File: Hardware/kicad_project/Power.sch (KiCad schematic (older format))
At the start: 11 parts

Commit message: update project with corrected schematic / pcb
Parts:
- removed U?: NCP1117-3.3_SOT223, Package_TO_SOT_SMD:SOT-223-3_TabPin2, symbol Regulator_Linear:NCP1117-3.3_SOT223
- added U7: AMS1117-3.3, TO_SOT_Packages_SMD:SOT-223, symbol Regulator_Linear:AMS1117-3.3
- C57: renamed from C?; footprint RandomJunk:C_0603_nosilk -> Capacitors_SMD:C_0402_NoSilk; LCSC c19702 -> C15525
- C58: renamed from C?; footprint (none) -> Capacitors_SMD:C_0402_NoSilk; LCSC (none) -> C15525
- Q1: renamed from Q?; LCSC c144153 -> C144153
- R16: renamed from R?; footprint Resistors_SMD:R_0603 -> Resistors_SMD:R_0402_NoSilk; LCSC c23162 -> C23162
- R17: renamed from R?; footprint Resistors_SMD:R_0603 -> Resistors_SMD:R_0402_NoSilk; LCSC c21190 -> C11702
- R18: renamed from R?; footprint Resistors_SMD:R_0603 -> Resistors_SMD:R_0402_NoSilk; LCSC c25803 -> C25803
- gave numbers to parts that had none: 4
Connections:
- net +3V3: now also U7.2 (VO)
- net +BATT: now also J7.2 (Pin_2); no longer J7.1 (Pin_1)
- net GND: now also J7.1 (Pin_1), U7.1 (GND); no longer J7.2 (Pin_2)
- net at D53.1 (K), Q1.2 (S): now also U7.3 (VI)
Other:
- moved on the sheet: J7
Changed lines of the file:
@@
 $EndDescr
 $Comp
-L power:+BATT #PWR?
+L power:+BATT #PWR041
 U 1 1 63689321
 P 7300 2550
-F 0 "#PWR?" H 7300 2400 50  0001 C CNN
+F 0 "#PWR041" H 7300 2400 50  0001 C CNN
 F 1 "+BATT" H 7315 2723 50  0000 C CNN
 F 2 "" H 7300 2550 50  0001 C CNN
@@
 	7700 3250 8050 3250
 $Comp
-L power:GND #PWR?
-U 1 1 6368932B
-P 8050 3800
-F 0 "#PWR?" H 8050 3550 50  0001 C CNN
-F 1 "GND" H 8055 3627 50  0000 C CNN
-F 2 "" H 8050 3800 50  0001 C CNN
-F 3 "" H 8050 3800 50  0001 C CNN
-	1    8050 3800
-	1    0    0    -1
-$EndComp
-$Comp
-L Device:C C?
+L Device:C C58
 U 1 1 63689331
 P 8050 3550
-F 0 "C?" H 8165 3596 50  0000 L CNN
+F 0 "C58" H 8165 3596 50  0000 L CNN
 F 1 "10u" H 8165 3505 50  0000 L CNN
-F 2 "" H 8088 3400 50  0001 C CNN
+F 2 "Capacitors_SMD:C_0402_NoSilk" H 8088 3400 50  0001 C CNN
 F 3 "~" H 8050 3550 50  0001 C CNN
+F 4 "C15525" H 8050 3550 50  0001 C CNN "LCSC"
 	1    8050 3550
 	1    0    0    -1
 $EndComp
 $Comp
-L power:+3.3V #PWR?
+L power:+3.3V #PWR045
 U 1 1 63689337
 P 8050 3250
-F 0 "#PWR?" H 8050 3100 50  0001 C CNN
+F 0 "#PWR045" H 8050 3100 50  0001 C CNN
 F 1 "+3.3V" H 8065 3423 50  0000 C CNN
 F 2 "" H 8050 3250 50  0001 C CNN
@@
 $EndComp
 $Comp
-L power:GND #PWR?
+L power:GND #PWR049
 U 1 1 6368933D
 P 7400 3550
-F 0 "#PWR?" H 7400 3300 50  0001 C CNN
+F 0 "#PWR049" H 7400 3300 50  0001 C CNN
 F 1 "GND" H 7405 3377 50  0000 C CNN
 F 2 "" H 7400 3550 50  0001 C CNN
@@
 	6900 3250 7100 3250
 $Comp
-L Regulator_Linear:NCP1117-3.3_SOT223 U?
-U 1 1 63689345
-P 7400 3250
-F 0 "U?" H 7400 3492 50  0000 C CNN
-F 1 "NCP1117-3.3_SOT223" H 7400 3401 50  0000 C CNN
-F 2 "Package_TO_SOT_SMD:SOT-223-3_TabPin2" H 7400 3450 50  0001 C CNN
-F 3 "http://www.onsemi.com/pub_link/Collateral/NCP1117-D.PDF" H 7500 3000 50  0001 C CNN
-	1    7400 3250
-	1    0    0    -1
-$EndComp
-$Comp
-L power:+BATT #PWR?
+L power:+BATT #PWR046
 U 1 1 6368934B
-P 3150 3550
-F 0 "#PWR?" H 3150 3400 50  0001 C CNN
-F 1 "+BATT" H 3165 3723 50  0000 C CNN
-F 2 "" H 3150 3550 50  0001 C CNN
-F 3 "" H 3150 3550 50  0001 C CNN
-	1    3150 3550
-	1    0    0    -1
-$EndComp
-$Comp
-L power:GND #PWR?
+P 3150 3700
+F 0 "#PWR046" H 3150 3550 50  0001 C CNN
+F 1 "+BATT" H 3165 3873 50  0000 C CNN
+F 2 "" H 3150 3700 50  0001 C CNN
+F 3 "" H 3150 3700 50  0001 C CNN
+	1    3150 3700
+	-1   0    0    1
+$EndComp
+$Comp
+L power:GND #PWR050
 U 1 1 63689351
-P 3150 3650
-F 0 "#PWR?" H 3150 3400 50  0001 C CNN
-F 1 "GND" H 3155 3477 50  0000 C CNN
-F 2 "" H 3150 3650 50  0001 C CNN
-F 3 "" H 3150 3650 50  0001 C CNN
-	1    3150 3650
-	1    0    0    -1
-$EndComp
-$Comp
-L Connector_Generic:Conn_01x02 J?
+P 3150 3600
+F 0 "#PWR050" H 3150 3350 50  0001 C CNN
+F 1 "GND" H 3155 3427 50  0000 C CNN
+F 2 "" H 3150 3600 50  0001 C CNN
+F 3 "" H 3150 3600 50  0001 C CNN
+	1    3150 3600
+	-1   0    0    1
+$EndComp
+$Comp
+L Connector_Generic:Conn_01x02 J7
 U 1 1 63689357
-P 3350 3550
-F 0 "J?" H 3430 3542 50  0000 L CNN
-F 1 "battery" H 3430 3451 50  0000 L CNN
-F 2 "Connectors_JST:JST_PH_B2B-PH-SM4-TB_02x2.00mm_Straight" H 3350 3550 50  0001 C CNN
-F 3 "~" H 3350 3550 50  0001 C CNN
-	1    3350 3550
-	1    0    0    -1
-$EndComp
-$Comp
-L Device:R_US R?
+P 3350 3600
+F 0 "J7" H 3430 3592 50  0000 L CNN
+F 1 "battery" H 3430 3501 50  0000 L CNN
+F 2 "Connectors_JST:JST_PH_B2B-PH-SM4-TB_02x2.00mm_Straight" H 3350 3600 50  0001 C CNN
+F 3 "~" H 3350 3600 50  0001 C CNN
+	1    3350 3600
+	1    0    0    -1
+$EndComp
+$Comp
+L Device:R_US R18
 U 1 1 6368935E
 P 6550 3400
-F 0 "R?" V 6345 3400 50  0000 C CNN
+F 0 "R18" V 6345 3400 50  0000 C CNN
 F 1 "100k" V 6436 3400 50  0000 C CNN
-F 2 "Resistors_SMD:R_0603" V 6590 3390 50  0001 C CNN
+F 2 "Resistors_SMD:R_0402_NoSilk" V 6590 3390 50  0001 C CNN
 F 3 "~" H 6550 3400 50  0001 C CNN
-F 4 "c25803" H 6550 3400 50  0001 C CNN "LCSC"
+F 4 "C25803" H 6550 3400 50  0001 C CNN "LCSC"
 	1    6550 3400
 	-1   0    0    1
@@
 Connection ~ 6550 3250
 $Comp
-L power:GND #PWR?
+L power:GND #PWR048
 U 1 1 63689365
 P 6550 3550
-F 0 "#PWR?" H 6550 3300 50  0001 C CNN
+F 0 "#PWR048" H 6550 3300 50  0001 C CNN
 F 1 "GND" H 6555 3377 50  0000 C CNN
 F 2 "" H 6550 3550 50  0001 C CNN
@@
 $EndComp
 $Comp
-L Device:R_US R?
+L Device:R_US R16
 U 1 1 6368936C
 P 4250 3350
-F 0 "R?" V 4045 3350 50  0000 C CNN
+F 0 "R16" V 4045 3350 50  0000 C CNN
 F 1 "4.7k" V 4136 3350 50  0000 C CNN
-F 2 "Resistors_SMD:R_0603" V 4290 3340 50  0001 C CNN
+F 2 "Resistors_SMD:R_0402_NoSilk" V 4290 3340 50  0001 C CNN
 F 3 "~" H 4250 3350 50  0001 C CNN
-F 4 "c23162" H 4250 3350 50  0001 C CNN "LCSC"
+F 4 "C23162" H 4250 3350 50  0001 C CNN "LCSC"
 	1    4250 3350
 	0    1    1    0
@@
 	4100 3350 4100 3650
 $Comp
-L dk_PMIC-Battery-Chargers:MCP73831T-2ATI_OT U?
+L dk_PMIC-Battery-Chargers:MCP73831T-2ATI_OT U6
 U 1 1 6368937D
 P 4800 3250
-F 0 "U?" H 4800 3653 60  0000 C CNN
+F 0 "U6" H 4800 3653 60  0000 C CNN
 F 1 "MCP73831T-2ATI_OT" H 4800 3547 60  0000 C CNN
 F 2 "TO_SOT_Packages_SMD:SOT-23-5" H 5000 3450 60  0001 L CNN
@@
 	6550 2850 6550 3250
 $Comp
-L Device:D_Schottky D?
+L Device:D_Schottky D53
 U 1 1 6368938B
 P 6700 3250
-F 0 "D?" H 6700 3034 50  0000 C CNN
+F 0 "D53" H 6700 3034 50  0000 C CNN
 F 1 "D_Schottky" H 6700 3125 50  0000 C CNN
 F 2 "Diodes_SMD:D_SMA" H 6700 3250 50  0001 C CNN
@@
 $EndComp
 $Comp
-L dk_Transistors-FETs-MOSFETs-Single:DMG2305UX-13 Q?
+L dk_Transistors-FETs-MOSFETs-Single:DMG2305UX-13 Q1
 U 1 1 6368939B
 P 7300 2750
-F 0 "Q?" H 7408 2803 60  0000 L CNN
+F 0 "Q1" H 7408 2803 60  0000 L CNN
 F 1 "DMG2305UX-13" H 7408 2697 60  0000 L CNN
 F 2 "digikey-footprints:SOT-23-3" H 7500 2950 60  0001 L CNN
@@
 F 11 "Diodes Incorporated" H 7500 3850 60  0001 L CNN "Manufacturer"
 F 12 "Active" H 7500 3950 60  0001 L CNN "Status"
-F 13 "c144153" H 7300 2750 50  0001 C CNN "LCSC"
+F 13 "C144153" H 7300 2750 50  0001 C CNN "LCSC"
 	1    7300 2750
 	1    0    0    -1
 $EndComp
 $Comp
-L power:VBUS #PWR?
+L power:VBUS #PWR043
 U 1 1 636893A1
 P 6550 2850
-F 0 "#PWR?" H 6550 2700 50  0001 C CNN
+F 0 "#PWR043" H 6550 2700 50  0001 C CNN
 F 1 "VBUS" H 6565 3023 50  0000 C CNN
 F 2 "" H 6550 2850 50  0001 C CNN
@@
 	5200 3250 6000 3250
 $Comp
-L power:GND #PWR?
+L power:GND #PWR047
 U 1 1 636893A9
 P 6000 3550
-F 0 "#PWR?" H 6000 3300 50  0001 C CNN
+F 0 "#PWR047" H 6000 3300 50  0001 C CNN
 F 1 "GND" H 6005 3377 50  0000 C CNN
 F 2 "" H 6000 3550 50  0001 C CNN
@@
 $EndComp
 $Comp
-L Device:C C?
+L Device:C C57
 U 1 1 636893B0
 P 6000 3400
-F 0 "C?" H 6115 3446 50  0000 L CNN
+F 0 "C57" H 6115 3446 50  0000 L CNN
 F 1 "10u" H 6115 3355 50  0000 L CNN
-F 2 "RandomJunk:C_0603_nosilk" H 6038 3250 50  0001 C CNN
+F 2 "Capacitors_SMD:C_0402_NoSilk" H 6038 3250 50  0001 C CNN
 F 3 "~" H 6000 3400 50  0001 C CNN
-F 4 "c19702" H 6000 3400 50  0001 C CNN "LCSC"
+F 4 "C15525" H 6000 3400 50  0001 C CNN "LCSC"
 	1    6000 3400
 	1    0    0    -1
 $EndComp
 $Comp
-L power:+BATT #PWR?
+L power:+BATT #PWR044
 U 1 1 636893B6
 P 6000 3250
-F 0 "#PWR?" H 6000 3100 50  0001 C CNN
+F 0 "#PWR044" H 6000 3100 50  0001 C CNN
 F 1 "+BATT" H 6015 3423 50  0000 C CNN
 F 2 "" H 6000 3250 50  0001 C CNN
@@
 	4800 2750 5800 2750
 $Comp
-L Device:LED D?
+L Device:LED D54
 U 1 1 636893C0
 P 5650 3350
-F 0 "D?" H 5643 3566 50  0000 C CNN
+F 0 "D54" H 5643 3566 50  0000 C CNN
 F 1 "LED" H 5643 3475 50  0000 C CNN
 F 2 "LEDs:LED_0603" H 5650 3350 50  0001 C CNN
@@
 $EndComp
 $Comp
-L Device:R_US R?
+L Device:R_US R17
 U 1 1 636893C7
 P 5350 3350
-F 0 "R?" V 5145 3350 50  0000 C CNN
+F 0 "R17" V 5145 3350 50  0000 C CNN
 F 1 "1k" V 5236 3350 50  0000 C CNN
-F 2 "Resistors_SMD:R_0603" V 5390 3340 50  0001 C CNN
+F 2 "Resistors_SMD:R_0402_NoSilk" V 5390 3340 50  0001 C CNN
 F 3 "~" H 5350 3350 50  0001 C CNN
-F 4 "c21190" H 5350 3350 50  0001 C CNN "LCSC"
+F 4 "C11702" H 5350 3350 50  0001 C CNN "LCSC"
 	1    5350 3350
 	0    1    1    0
@@
 	4800 3050 4800 2750
 $Comp
-L power:VBUS #PWR?
+L power:VBUS #PWR042
 U 1 1 636893CE
 P 4800 2750
-F 0 "#PWR?" H 4800 2600 50  0001 C CNN
+F 0 "#PWR042" H 4800 2600 50  0001 C CNN
 F 1 "VBUS" H 4815 2923 50  0000 C CNN
 F 2 "" H 4800 2750 50  0001 C CNN
@@
 	4100 3650 4800 3650
 $Comp
-L power:GND #PWR?
+L power:GND #PWR051
 U 1 1 636893D5
 P 4800 3650
-F 0 "#PWR?" H 4800 3400 50  0001 C CNN
+F 0 "#PWR051" H 4800 3400 50  0001 C CNN
 F 1 "GND" H 4805 3477 50  0000 C CNN
 F 2 "" H 4800 3650 50  0001 C CNN
@@
 	1    0    0    -1
 $EndComp
+$Comp
+L Regulator_Linear:AMS1117-3.3 U7
+U 1 1 616EA29F
+P 7400 3250
+F 0 "U7" H 7400 3492 50  0000 C CNN
+F 1 "AMS1117-3.3" H 7400 3401 50  0000 C CNN
+F 2 "TO_SOT_Packages_SMD:SOT-223" H 7400 3450 50  0001 C CNN
+F 3 "http://www.advanced-monolithic.com/pdf/ds1117.pdf" H 7500 3000 50  0001 C CNN
+F 4 "C6186" H 7400 3250 50  0001 C CNN "LCSC"
+	1    7400 3250
+	1    0    0    -1
+$EndComp
+$Comp
+L power:GND #PWR052
+U 1 1 6368932B
+P 8050 3800
+F 0 "#PWR052" H 8050 3550 50  0001 C CNN
+F 1 "GND" H 8055 3627 50  0000 C CNN
+F 2 "" H 8050 3800 50  0001 C CNN
+F 3 "" H 8050 3800 50  0001 C CNN
+	1    8050 3800
+	1    0    0    -1
+$EndComp

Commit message: initial firmware commit, update hardware
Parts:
- R16: LCSC C23162 -> C25900
- R18: LCSC C25803 -> C25741
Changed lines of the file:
@@
 F 2 "Resistors_SMD:R_0402_NoSilk" V 6590 3390 50  0001 C CNN
 F 3 "~" H 6550 3400 50  0001 C CNN
-F 4 "C25803" H 6550 3400 50  0001 C CNN "LCSC"
+F 4 "C25741" H 6550 3400 50  0001 C CNN "LCSC"
 	1    6550 3400
 	-1   0    0    1
@@
 F 2 "Resistors_SMD:R_0402_NoSilk" V 4290 3340 50  0001 C CNN
 F 3 "~" H 4250 3350 50  0001 C CNN
-F 4 "C23162" H 4250 3350 50  0001 C CNN "LCSC"
+F 4 "C25900" H 4250 3350 50  0001 C CNN "LCSC"
 	1    4250 3350
 	0    1    1    0

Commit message: final v6 schematic
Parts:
- U7: LCSC C6186 -> C140704
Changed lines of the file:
@@
 F 2 "TO_SOT_Packages_SMD:SOT-223" H 7400 3450 50  0001 C CNN
 F 3 "http://www.advanced-monolithic.com/pdf/ds1117.pdf" H 7500 3000 50  0001 C CNN
-F 4 "C6186" H 7400 3250 50  0001 C CNN "LCSC"
+F 4 "C140704" H 7400 3250 50  0001 C CNN "LCSC"
 	1    7400 3250
 	1    0    0    -1

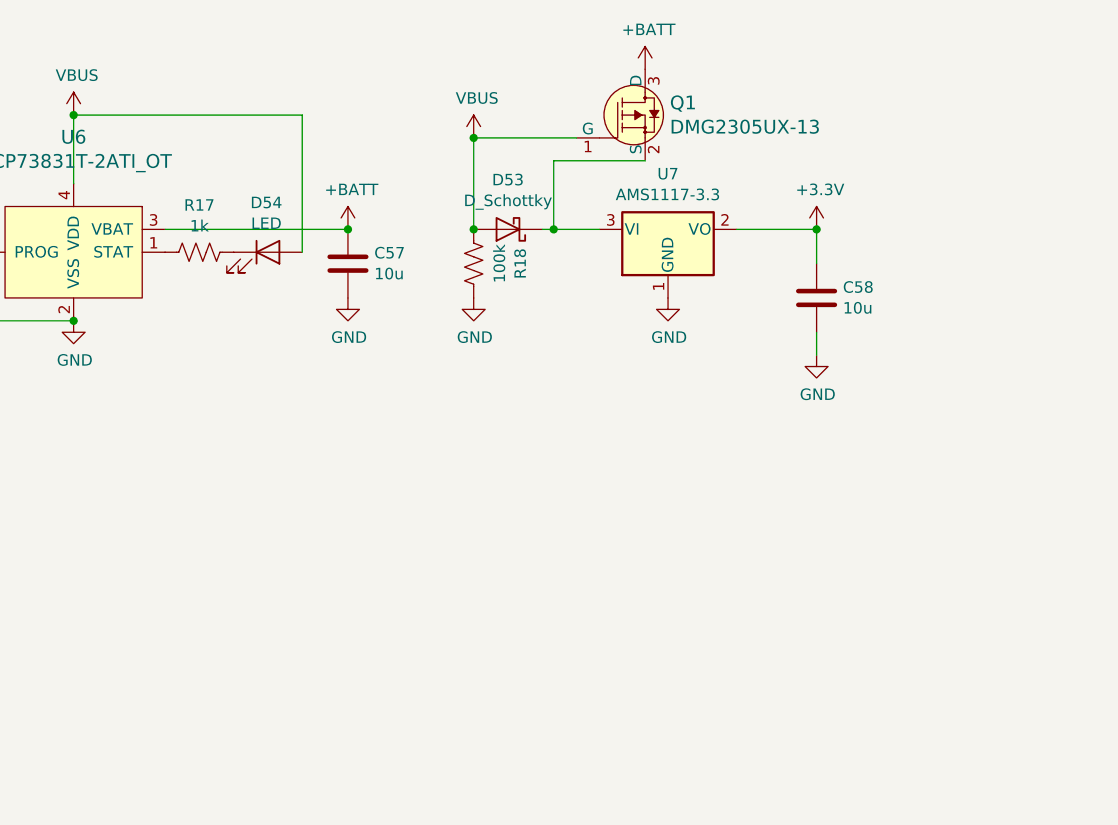
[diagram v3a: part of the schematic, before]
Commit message: new hardware rev
- soft / latching power switch
- corrected mic
- added pullup to flash ss
- front & back enclosure plates
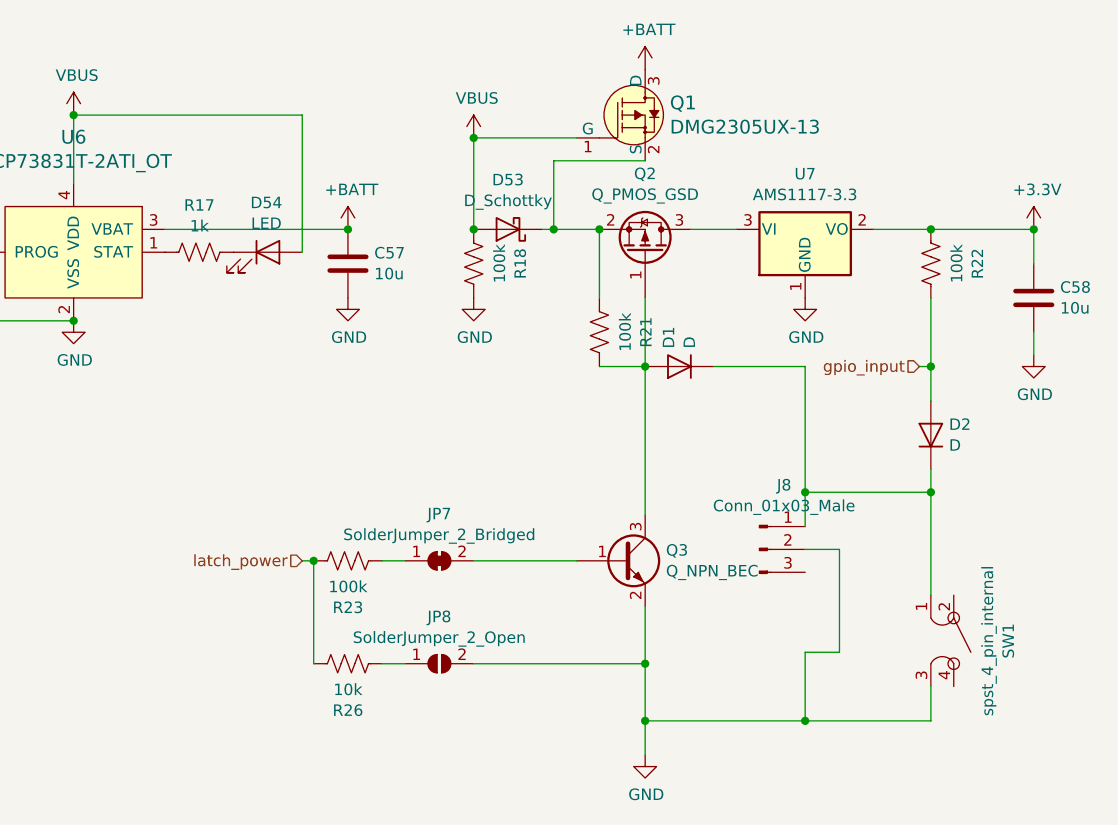
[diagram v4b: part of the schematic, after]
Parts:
- added D1, D2: D, RandomJunk:D_SOD-323F_less_silk, symbol Device:D
- added J8: Conn_01x03_Male, Connector_PinHeader_2.54mm:PinHeader_1x03_P2.54mm_Horizontal, symbol Connector:Conn_01x03_Male
- added JP7: SolderJumper_2_Bridged, Jumper:SolderJumper-2_P1.3mm_Bridged_RoundedPad1.0x1.5mm, symbol Jumper:SolderJumper_2_Bridged
- added JP8: SolderJumper_2_Open, Jumper:SolderJumper-2_P1.3mm_Open_RoundedPad1.0x1.5mm, symbol Jumper:SolderJumper_2_Open
- added Q2: Q_PMOS_GSD, TO_SOT_Packages_SMD:SOT-23, symbol Device:Q_PMOS_GSD
- added Q3: Q_NPN_BEC, TO_SOT_Packages_SMD:SOT-23, symbol Device:Q_NPN_BEC
- added R21, R22, R23: 100k, Resistors_SMD:R_0402_NoSilk, symbol Device:R_US
- added R26: 10k, Resistors_SMD:R_0402_NoSilk, symbol Device:R_US
- added SW1: spst_4_pin_internal, RandomJunk:ts1102_smallerpads_buttonhole, symbol customLibrary:spst_4_pin_internal
- J7: footprint Connectors_JST:JST_PH_B2B-PH-SM4-TB_02x2.00mm_Straight -> Connectors_JST:JST_PH_S2B-PH-SM4-TB_02x2.00mm_Angled
- R18: LCSC C25741 -> C25086
- U7: LCSC C140704 -> C6186
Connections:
- net +3V3: now also R22.2
- net GND: now also J8.2 (Pin_2), JP8.2 (B), Q3.2 (E), SW1.3
- net at D53.1 (K), Q1.2 (S): now also Q2.2 (S), R21.2; no longer U7.3 (VI)
- new net: Q2.3 (D), U7.3 (VI)
- new net: D1.2 (A), Q2.1 (G), Q3.3 (C), R21.1
- new net: JP7.2 (B), Q3.1 (B)
- new net: JP7.1 (A), R23.2
- new net: D1.1 (K), D2.1 (K), J8.1 (Pin_1), SW1.1
- new net: JP8.1 (A), R26.2
- new net gpio_input: D2.2 (A), R22.1
- new net latch_power: R23.1, R26.1
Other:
- moved on the sheet: C58, U7
